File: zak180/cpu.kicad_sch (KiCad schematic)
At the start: 1 part, among them IC1 Z8-L180-S180-180-PLCC-68

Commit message: HW: Further work on schematic
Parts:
- added C38, C39: 22p, Capacitor_THT:C_Disc_D4.3mm_W1.9mm_P5.00mm, symbol Device:C
- added C40, C41, C42, C43, C45, C46, C47, C48: 100n, Capacitor_THT:C_Disc_D5.0mm_W2.5mm_P2.50mm, symbol Device:C
- added RN2: 47K, Resistor_THT:R_Array_SIP9, symbol Device:R_Network08
- added U16: 74HC08, Package_DIP:DIP-14_W7.62mm, symbol 74xx:74LS08
- added U20, U21: 74HC688, symbol 74xx:74HC688
- added U23: 74HC74, symbol 74xx:74HC74
- added U24: 74HC02, symbol 74xx:74HC02
- added U8: 74HC138, symbol 74xx:74HC138
- added Y2: 16 MHz, Crystal:Crystal_HC49-4H_Vertical, symbol Device:Crystal
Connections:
- net GND: now also C38.1, C39.1, C40.2, C41.2, C42.2, C43.2, C45.2, C46.2, C47.2, C48.2, U20.10 (GND), U20.12 (R4), U20.14 (R5), U20.16 (R6), U20.18 (R7), U20.2 (P0), U20.3 (R0), U20.4 (P1), U20.5 (R1), U20.7 (R2), U20.9 (R3), U21.10 (GND), U23.12 (D), U23.7 (GND), U24.7 (GND), U8.5 (~{E1}), U8.8 (GND)
- net VCC: now also C40.1, C41.1, C42.1, C43.1, C45.1, C46.1, C47.1, C48.1, RN2.1 (common), U20.20 (VCC), U21.12 (R4), U21.14 (R5), U21.16 (R6), U21.18 (R7), U21.2 (P0), U21.20 (VCC), U21.3 (R0), U21.5 (R1), U21.7 (R2), U21.9 (R3), U23.13 (~{R}), U23.14 (VCC), U23.4 (~{S}), U24.14 (VCC), U8.16 (VCC)
- net ~{INT0}: now reaches IC1.10 (~{INT0})
- net ~{INT0}: now also RN2.8 (R7)
- net ~{INT1}: now reaches IC1.11 (~{INT1})
- net ~{INT1}: now also RN2.7 (R6)
- net at IC1.12 (~{INT2}): now also RN2.6 (R5), U23.9 (Q)
- net A0: now reaches IC1.14 (A0)
- net A1: now reaches IC1.15 (A1)
- net A2: now reaches IC1.16 (A2)
- net A3: now reaches IC1.17 (A3)
- net A4: now reaches IC1.19 (A4)
- net A5: now reaches IC1.20 (A5)
- net A5: now also U8.3 (A2)
- net A6: now reaches IC1.21 (A6)
- net A6: now also U8.2 (A1)
- net A7: now reaches IC1.22 (A7)
- net A7: now also U8.1 (A0)
- net A8: now reaches IC1.23 (A8)
- net A9: now reaches IC1.24 (A9)
- net A10: now reaches IC1.25 (A10)
- net A11: now reaches IC1.26 (A11)
- net A12: now reaches IC1.27 (A12)
- net A13: now reaches IC1.28 (A13)
- net A13: now also U21.4 (P1)
- net A14: now reaches IC1.29 (A14)
- net A14: now also U20.6 (P2), U21.6 (P2)
- net at IC1.3 (XTAL): now also C38.2, Y2.1
- net A15: now reaches IC1.30 (A15)
- net A15: now also U20.8 (P3), U21.8 (P3)
- net A16: now reaches IC1.31 (A16)
- net A16: now also U20.11 (P4), U21.11 (P4)
- net A17: now reaches IC1.32 (A17)
- net A17: now also U20.13 (P5), U21.13 (P5)
- net A18: now reaches IC1.33 (A18/TOUT)
- net A18: now also U20.15 (P6), U21.15 (P6)
- net A19: now reaches IC1.35 (A19)
- net A19: now also U20.17 (P7), U21.17 (P7)
- net D0: now reaches IC1.37 (D0)
- net D0: now also U23.2 (D)
- net D1: now reaches IC1.38 (D1)
- net D2: now reaches IC1.39 (D2)
- net at IC1.4 (EXTAL): now also C39.2, Y2.2
- net D3: now reaches IC1.40 (D3)
- net D4: now reaches IC1.41 (D4)
- net D5: now reaches IC1.42 (D5)
- net D6: now reaches IC1.43 (D6)
- net D7: now reaches IC1.44 (D7)
- net TX0: now reaches IC1.48 (TXA0)
- net RX0: now reaches IC1.49 (RXA0)
- net ~{WAIT}: now reaches IC1.5 (~{WAIT})
- net ~{WAIT}: now also RN2.5 (R4)
- net ~{DREQ0}: now reaches IC1.50 (CKA0/~{DREQ0})
- net ~{DREQ0}: now also RN2.3 (R2)
- net TX1: now reaches IC1.51 (TXA1)
- net RX1: now reaches IC1.53 (RXA1)
- net ~{TEND0}: now reaches IC1.54 (CKA1/~{TEND0})
- net ~{DREQ1}: now reaches IC1.58 (~{DREQ1})
- net ~{DREQ1}: now also RN2.2 (R1)
- net ~{TEND1}: now reaches IC1.59 (~{TEND1})
- net ~{BUSACK}: now reaches IC1.6 (~{BUSACK})
- net ~{HALT}: now reaches IC1.60 (~{HALT})
- net ~{RFSH}: now reaches IC1.61 (~{RFSH})
- net ~{IORQ}: now reaches IC1.62 (~{IORQ})
- net ~{IORQ}: now also U8.4 (~{E0})
- net at IC1.63 (~{MREQ}): now also U20.1 (G), U21.1 (G), U24.8, U24.9
- net ~{M1}: now reaches IC1.65 (~{M1})
- net ~{M1}: now also U8.6 (E2)
- net ~{WR}: now reaches IC1.66 (~{WR})
- net ~{RD}: now reaches IC1.67 (~{RD})
- net CLK: now reaches IC1.68 (PHI)
- net ~{BUSREQ}: now reaches IC1.7 (~{BUSREQ})
- net ~{BUSREQ}: now also RN2.4 (R3)
- net ~{RST}: now reaches IC1.8 (~{RESET})
- net ~{RST}: now also U23.1 (~{R})
- net ~{NMI}: now reaches IC1.9 (~{NMI})
- net ~{NMI}: now also RN2.9 (R8)
- new net: U23.3 (C), U8.12 (~{Y3})
- new net: U23.5 (Q), U24.3
- new net: U24.1, U24.5, U24.6
- new net: U20.19 (P=R), U24.2
- new net: U16.9, U24.10
- new net: U16.10, U16.6
- new net: U16.8, U24.11, U24.12
- new net: U23.10 (~{S}), U8.13 (~{Y2})
- new net VBLANK: U23.11 (C)
- new net ~{FLOPPY}: U8.7 (~{Y7})
- new net ~{KEYBOARD}: U8.11 (~{Y4})
- new net ~{PIO}: U8.10 (~{Y5})
- new net ~{RAM}: U24.13
- new net ~{ROM}: U16.5, U24.4
- new net ~{SOUND}: U8.9 (~{Y6})
- new net ~{VRAM}: U16.4, U21.19 (P=R)
- no-connect marks 0 -> 12
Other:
- note added: "Internal I/O"
- moved on the sheet: IC1

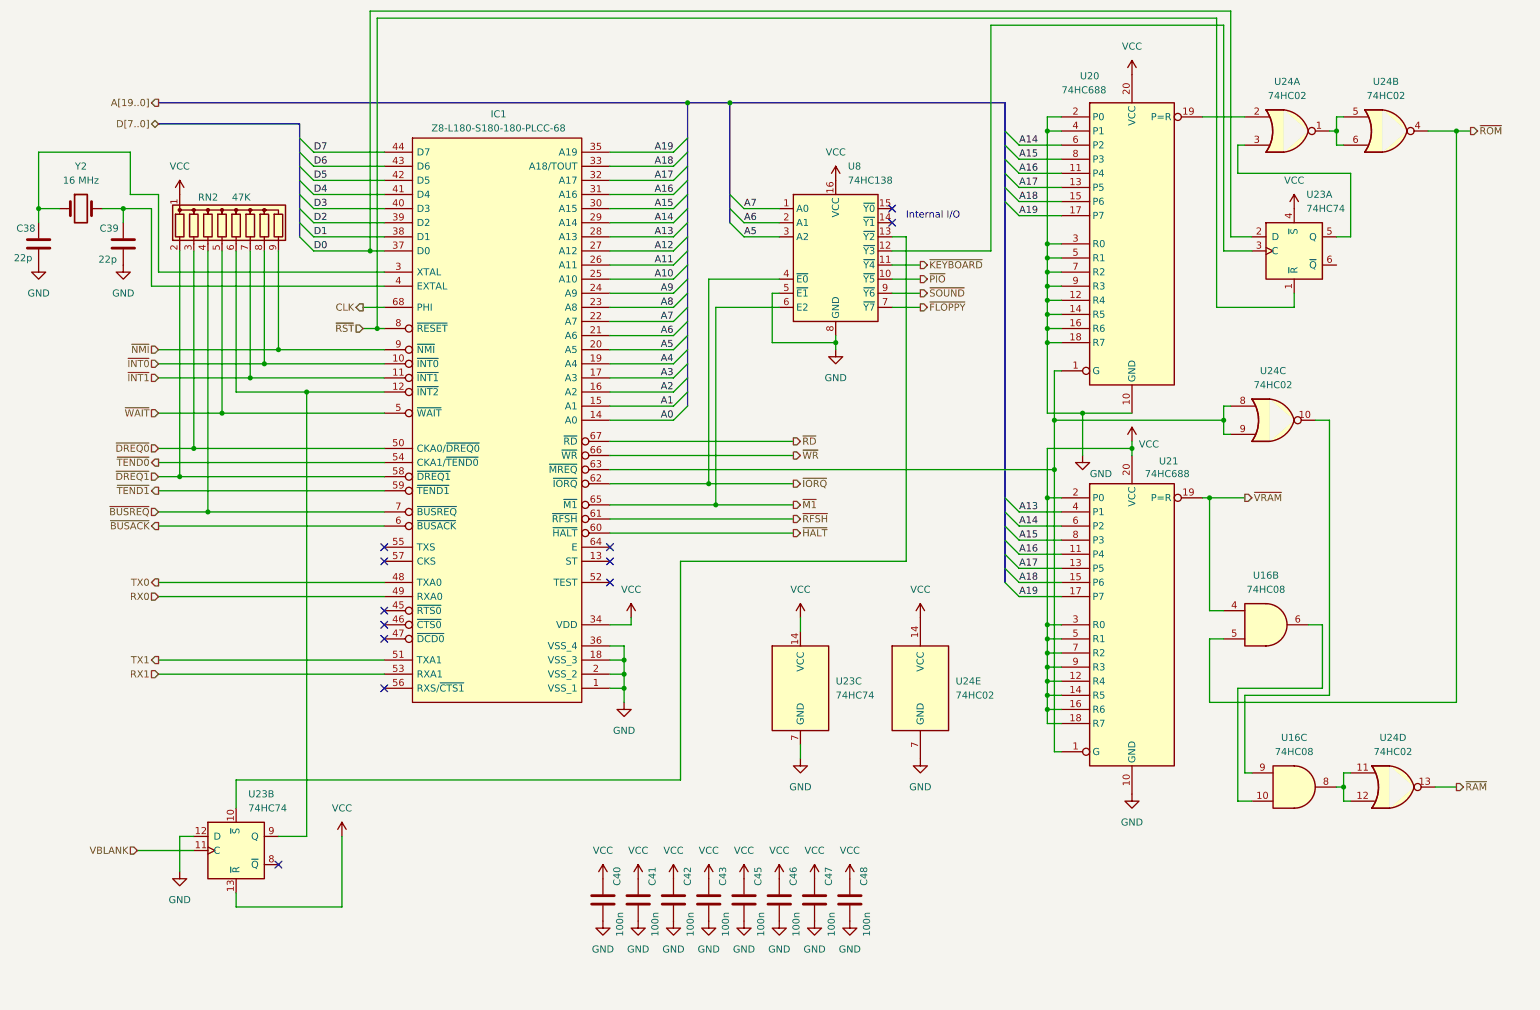
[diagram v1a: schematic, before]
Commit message: HW: Add memory, serial and power
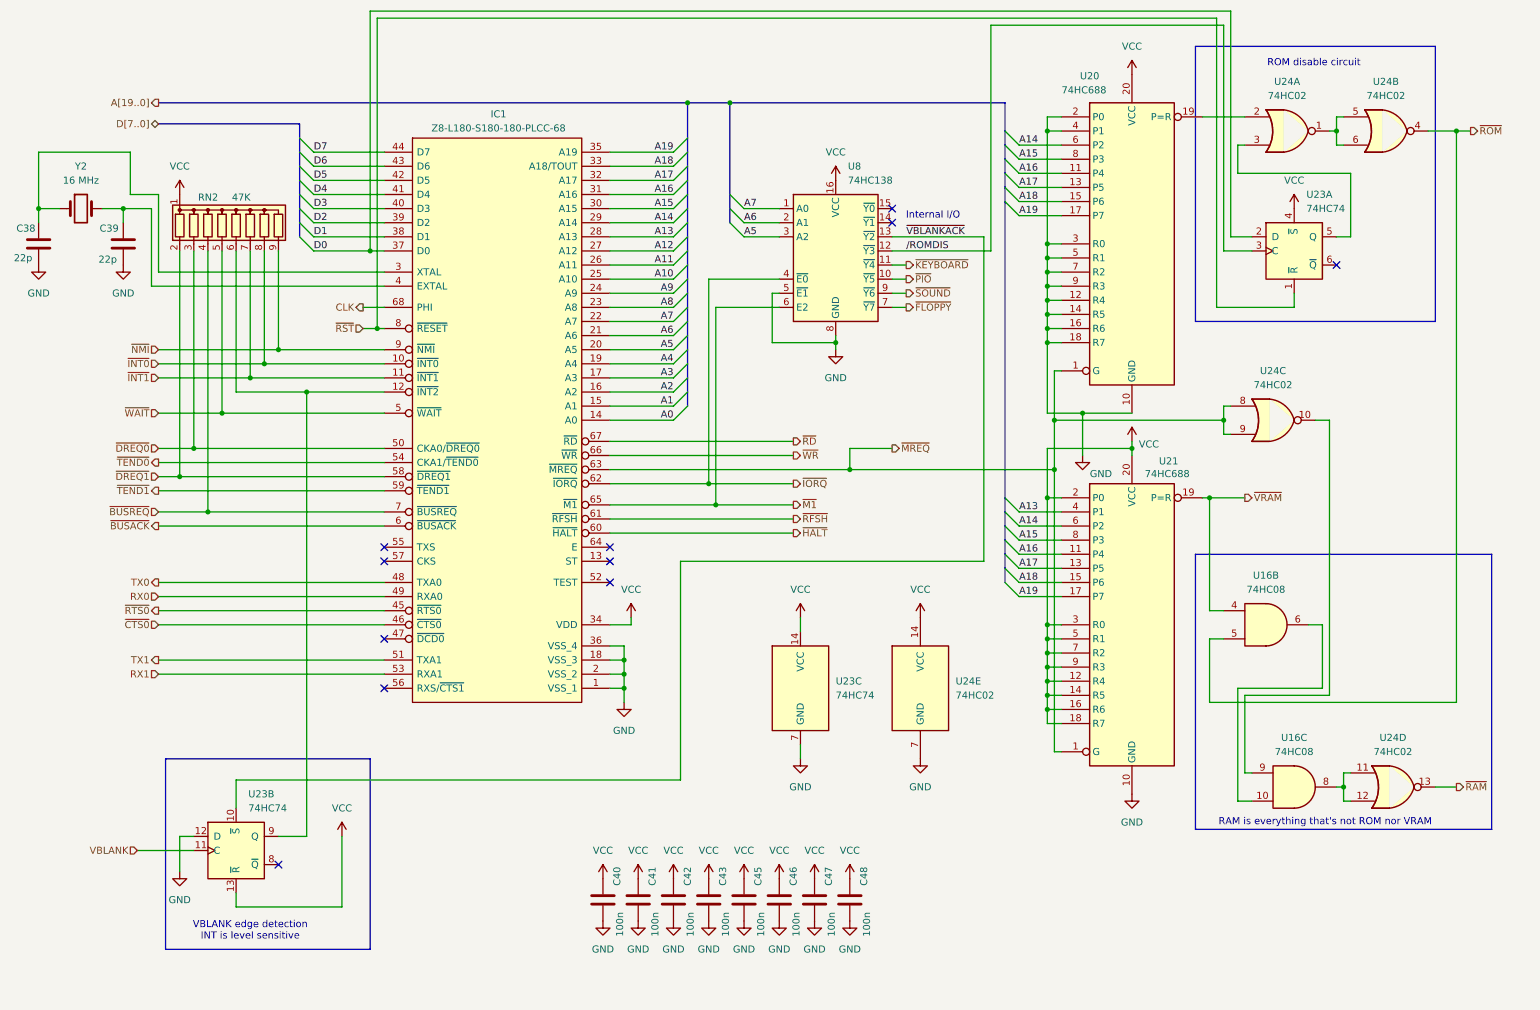
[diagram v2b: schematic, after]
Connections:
- net /ROMDIS: now reaches U23.3 (C), U8.12 (~{Y3})
- net ~{MREQ}: now reaches IC1.63 (~{MREQ}), U20.1 (G), U21.1 (G), U24.8, U24.9
- net ~{RTS0}: now reaches IC1.45 (~{RTS0})
- net ~{CTS0}: now reaches IC1.46 (~{CTS0})
- net ~{VBLANKACK}: now reaches U23.10 (~{S}), U8.13 (~{Y2})
- no-connect marks 12 -> 11
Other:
- note added: "RAM is everything that's not ROM nor VRAM"
- note added: "ROM disable circuit"
- note added: "VBLANK edge detection INT is level sensitive"
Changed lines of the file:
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@@
 	)
 	(junction
+		(at 165.1 100.33)
+		(diameter 0)
+		(color 0 0 0 0)
+	)
+	(junction
 		(at 201.93 100.33)
 		(diameter 0)
@@
 	)
 	(no_connect
-		(at 81.28 125.73)
+		(at 81.28 114.3)
 	)
 	(no_connect
-		(at 81.28 114.3)
+		(at 252.73 63.5)
 	)
 	(no_connect
@@
 		(at 121.92 116.84)
 	)
-	(no_connect
-		(at 81.28 128.27)
-	)
 	(bus_entry
 		(at 66.04 55.88)
@@
 	(wire
 		(pts
+			(xy 165.1 100.33) (xy 165.1 96.52)
+		)
+		(stroke
+			(width 0)
+			(type default)
+		)
+	)
+	(wire
+		(pts
 			(xy 251.46 39.37) (xy 252.73 39.37)
 		)
@@
 	(wire
 		(pts
-			(xy 172.72 58.42) (xy 175.26 58.42)
+			(xy 172.72 58.42) (xy 189.23 58.42)
 		)
 		(stroke
@@
 	(wire
 		(pts
+			(xy 165.1 96.52) (xy 172.72 96.52)
+		)
+		(stroke
+			(width 0)
+			(type default)
+		)
+	)
+	(wire
+		(pts
 			(xy 121.92 111.76) (xy 154.94 111.76)
 		)
@@
 	(wire
 		(pts
+			(xy 40.64 128.27) (xy 81.28 128.27)
+		)
+		(stroke
+			(width 0)
+			(type default)
+		)
+	)
+	(wire
+		(pts
 			(xy 195.58 52.07) (xy 203.2 52.07)
 		)
@@
 	(wire
 		(pts
-			(xy 177.8 71.12) (xy 172.72 71.12)
+			(xy 175.26 71.12) (xy 172.72 71.12)
 		)
 		(stroke
@@
 	(wire
 		(pts
-			(xy 175.26 58.42) (xy 175.26 116.84)
+			(xy 189.23 58.42) (xy 189.23 116.84)
 		)
 		(stroke
@@
 	(wire
 		(pts
+			(xy 40.64 125.73) (xy 81.28 125.73)
+		)
+		(stroke
+			(width 0)
+			(type default)
+		)
+	)
+	(wire
+		(pts
 			(xy 121.92 45.72) (xy 133.35 45.72)
 		)
@@
 	(wire
 		(pts
-			(xy 175.26 116.84) (xy 134.62 116.84)
+			(xy 189.23 116.84) (xy 134.62 116.84)
 		)
 		(stroke
@@
 	(wire
 		(pts
-			(xy 177.8 68.58) (xy 172.72 68.58)
+			(xy 175.26 68.58) (xy 172.72 68.58)
 		)
 		(stroke
@@
 	(wire
 		(pts
-			(xy 177.8 63.5) (xy 172.72 63.5)
+			(xy 175.26 63.5) (xy 172.72 63.5)
 		)
 		(stroke
@@
 	(wire
 		(pts
+			(xy 165.1 100.33) (xy 201.93 100.33)
+		)
+		(stroke
+			(width 0)
+			(type default)
+		)
+	)
+	(wire
+		(pts
 			(xy 140.97 106.68) (xy 154.94 106.68)
 		)
@@
 	(wire
 		(pts
-			(xy 177.8 66.04) (xy 172.72 66.04)
+			(xy 175.26 66.04) (xy 172.72 66.04)
 		)
 		(stroke
@@
 	(wire
 		(pts
-			(xy 121.92 100.33) (xy 201.93 100.33)
+			(xy 121.92 100.33) (xy 165.1 100.33)
 		)
 		(stroke
@@
 		)
 	)
+	(rectangle
+		(start 227.33 115.57)
+		(end 280.67 165.1)
+		(stroke
+			(width 0)
+			(type default)
+		)
+		(fill
+			(type none)
+		)
+	)
+	(rectangle
+		(start 227.33 24.13)
+		(end 270.51 73.66)
+		(stroke
+			(width 0)
+			(type default)
+		)
+		(fill
+			(type none)
+		)
+	)
+	(rectangle
+		(start 41.91 152.4)
+		(end 78.74 186.69)
+		(stroke
+			(width 0)
+			(type default)
+		)
+		(fill
+			(type none)
+		)
+	)
+	(text "RAM is everything that's not ROM nor VRAM"
+		(exclude_from_sim no)
+		(at 250.698 163.83 0)
+		(effects
+			(font
+				(size 1.27 1.27)
+			)
+		)
+	)
 	(text "Internal I/O"
 		(exclude_from_sim no)
@@
 		)
 	)
+	(text "ROM disable circuit"
+		(exclude_from_sim no)
+		(at 248.666 27.178 0)
+		(effects
+			(font
+				(size 1.27 1.27)
+			)
+		)
+	)
+	(text "VBLANK edge detection\nINT is level sensitive"
+		(exclude_from_sim no)
+		(at 57.15 183.388 0)
+		(effects
+			(font
+				(size 1.27 1.27)
+			)
+		)
+	)
 	(label "A1"
 		(at 133.35 88.9 180)
@@
 		)
 	)
+	(label "{slash}ROMDIS"
+		(at 175.26 60.96 0)
+		(fields_autoplaced yes)
+		(effects
+			(font
+				(size 1.27 1.27)
+			)
+			(justify left bottom)
+		)
+	)
 	(label "A5"
 		(at 146.05 58.42 0)
@@
 		)
 	)
+	(label "~{VBLANKACK}"
+		(at 175.26 58.42 0)
+		(fields_autoplaced yes)
+		(effects
+			(font
+				(size 1.27 1.27)
+			)
+			(justify left bottom)
+		)
+	)
 	(label "A15"
 		(at 195.58 44.45 0)
@@
 	(hierarchical_label "~{FLOPPY}"
 		(shape output)
-		(at 177.8 71.12 0)
+		(at 175.26 71.12 0)
 		(fields_autoplaced yes)
 		(effects
@@
 		)
 	)
+	(hierarchical_label "~{RTS0}"
+		(shape output)
+		(at 40.64 125.73 180)
+		(fields_autoplaced yes)
+		(effects
+			(font
+				(size 1.27 1.27)
+			)
+			(justify right)
+		)
+	)
 	(hierarchical_label "CLK"
 		(shape output)
@@
 		)
 	)
+	(hierarchical_label "~{CTS0}"
+		(shape input)
+		(at 40.64 128.27 180)
+		(fields_autoplaced yes)
+		(effects
+			(font
+				(size 1.27 1.27)
+			)
+			(justify right)
+		)
+	)
 	(hierarchical_label "A[19..0]"
 		(shape output)
@@
 	(hierarchical_label "~{KEYBOARD}"
 		(shape output)
-		(at 177.8 63.5 0)
+		(at 175.26 63.5 0)
 		(fields_autoplaced yes)
 		(effects
@@
 	(hierarchical_label "~{PIO}"
 		(shape output)
-		(at 177.8 66.04 0)
+		(at 175.26 66.04 0)
 		(fields_autoplaced yes)
 		(effects
@@
 		)
 	)
+	(hierarchical_label "~{MREQ}"
+		(shape output)
+		(at 172.72 96.52 0)
+		(fields_autoplaced yes)
+		(effects
+			(font
+				(size 1.27 1.27)
+			)
+			(justify left)
+		)
+	)
 	(hierarchical_label "~{SOUND}"
 		(shape output)
-		(at 177.8 68.58 0)
+		(at 175.26 68.58 0)
 		(fields_autoplaced yes)
 		(effects
